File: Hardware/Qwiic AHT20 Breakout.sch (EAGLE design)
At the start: 25 parts, among them J2 QWIIC_RIGHT_ANGLE, J3 PTH, J4 QWIIC_RIGHT_ANGLE, U2 AHT20QFN-6

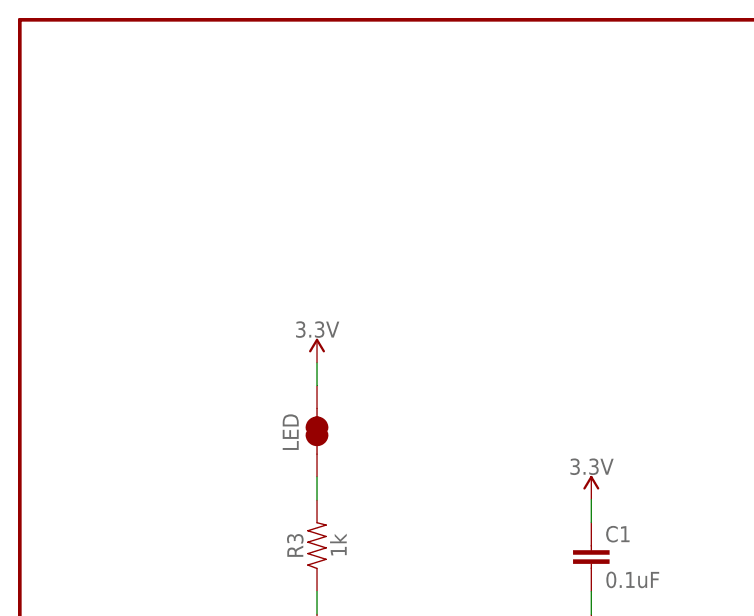
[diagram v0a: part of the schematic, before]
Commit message: Fix FP of IC to correct 2mm pad spacing
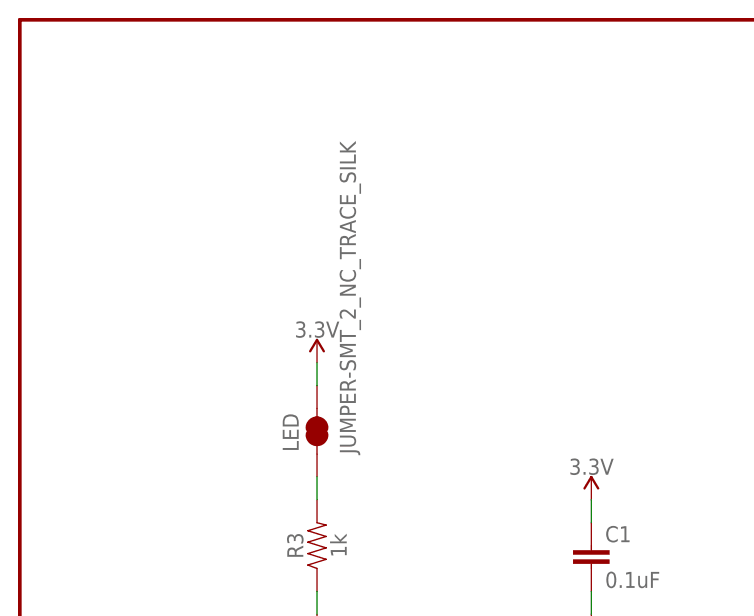
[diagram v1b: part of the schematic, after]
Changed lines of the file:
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@@
 <?xml version="1.0" encoding="utf-8"?>
 <!DOCTYPE eagle SYSTEM "eagle.dtd">
-<eagle version="9.5.2">
+<eagle version="9.6.0">
 <drawing>
 <settings>
@@
 <grid distance="0.1" unitdist="inch" unit="inch" style="lines" multiple="1" display="no" altdistance="0.01" altunitdist="inch" altunit="inch"/>
 <layers>
-<layer number="1" name="Top" color="4" fill="1" visible="yes" active="no"/>
-<layer number="2" name="Route2" color="1" fill="3" visible="yes" active="no"/>
-<layer number="3" name="Route3" color="4" fill="3" visible="yes" active="no"/>
-<layer number="4" name="Route4" color="1" fill="4" visible="yes" active="no"/>
-<layer number="5" name="Route5" color="4" fill="4" visible="yes" active="no"/>
-<layer number="6" name="Route6" color="1" fill="8" visible="yes" active="no"/>
-<layer number="7" name="Route7" color="4" fill="8" visible="yes" active="no"/>
-<layer number="8" name="Route8" color="1" fill="2" visible="yes" active="no"/>
-<layer number="9" name="Route9" color="4" fill="2" visible="yes" active="no"/>
-<layer number="10" name="Route10" color="1" fill="7" visible="yes" active="no"/>
-<layer number="11" name="Route11" color="4" fill="7" visible="yes" active="no"/>
-<layer number="12" name="Route12" color="1" fill="5" visible="yes" active="no"/>
-<layer number="13" name="Route13" color="4" fill="5" visible="yes" active="no"/>
-<layer number="14" name="Route14" color="1" fill="6" visible="yes" active="no"/>
-<layer number="15" name="Route15" color="4" fill="6" visible="yes" active="no"/>
-<layer number="16" name="Bottom" color="1" fill="1" visible="yes" active="no"/>
-<layer number="17" name="Pads" color="2" fill="1" visible="yes" active="no"/>
-<layer number="18" name="Vias" color="2" fill="1" visible="yes" active="no"/>
-<layer number="19" name="Unrouted" color="6" fill="1" visible="yes" active="no"/>
-<layer number="20" name="Dimension" color="24" fill="1" visible="yes" active="no"/>
-<layer number="21" name="tPlace" color="16" fill="1" visible="yes" active="no"/>
-<layer number="22" name="bPlace" color="14" fill="1" visible="yes" active="no"/>
-<layer number="23" name="tOrigins" color="15" fill="1" visible="yes" active="no"/>
-<layer number="24" name="bOrigins" color="15" fill="1" visible="yes" active="no"/>
-<layer number="25" name="tNames" color="7" fill="1" visible="yes" active="no"/>
-<layer number="26" name="bNames" color="7" fill="1" visible="yes" active="no"/>
-<layer number="27" name="tValues" color="7" fill="1" visible="yes" active="no"/>
-<layer number="28" name="bValues" color="7" fill="1" visible="yes" active="no"/>
+<layer number="1" name="Top" color="4" fill="1" visible="no" active="no"/>
+<layer number="2" name="Route2" color="1" fill="3" visible="no" active="no"/>
+<layer number="3" name="Route3" color="4" fill="3" visible="no" active="no"/>
+<layer number="4" name="Route4" color="1" fill="4" visible="no" active="no"/>
+<layer number="5" name="Route5" color="4" fill="4" visible="no" active="no"/>
+<layer number="6" name="Route6" color="1" fill="8" visible="no" active="no"/>
+<layer number="7" name="Route7" color="4" fill="8" visible="no" active="no"/>
+<layer number="8" name="Route8" color="1" fill="2" visible="no" active="no"/>
+<layer number="9" name="Route9" color="4" fill="2" visible="no" active="no"/>
+<layer number="10" name="Route10" color="1" fill="7" visible="no" active="no"/>
+<layer number="11" name="Route11" color="4" fill="7" visible="no" active="no"/>
+<layer number="12" name="Route12" color="1" fill="5" visible="no" active="no"/>
+<layer number="13" name="Route13" color="4" fill="5" visible="no" active="no"/>
+<layer number="14" name="Route14" color="1" fill="6" visible="no" active="no"/>
+<layer number="15" name="Route15" color="4" fill="6" visible="no" active="no"/>
+<layer number="16" name="Bottom" color="1" fill="1" visible="no" active="no"/>
+<layer number="17" name="Pads" color="2" fill="1" visible="no" active="no"/>
+<layer number="18" name="Vias" color="2" fill="1" visible="no" active="no"/>
+<layer number="19" name="Unrouted" color="6" fill="1" visible="no" active="no"/>
+<layer number="20" name="Dimension" color="24" fill="1" visible="no" active="no"/>
+<layer number="21" name="tPlace" color="16" fill="1" visible="no" active="no"/>
+<layer number="22" name="bPlace" color="14" fill="1" visible="no" active="no"/>
+<layer number="23" name="tOrigins" color="15" fill="1" visible="no" active="no"/>
+<layer number="24" name="bOrigins" color="15" fill="1" visible="no" active="no"/>
+<layer number="25" name="tNames" color="7" fill="1" visible="no" active="no"/>
+<layer number="26" name="bNames" color="7" fill="1" visible="no" active="no"/>
+<layer number="27" name="tValues" color="7" fill="1" visible="no" active="no"/>
+<layer number="28" name="bValues" color="7" fill="1" visible="no" active="no"/>
 <layer number="29" name="tStop" color="7" fill="3" visible="no" active="no"/>
 <layer number="30" name="bStop" color="7" fill="6" visible="no" active="no"/>
@@
 <layer number="35" name="tGlue" color="7" fill="4" visible="no" active="no"/>
 <layer number="36" name="bGlue" color="7" fill="5" visible="no" active="no"/>
-<layer number="37" name="tTest" color="7" fill="1" visible="yes" active="no"/>
-<layer number="38" name="bTest" color="7" fill="1" visible="yes" active="no"/>
+<layer number="37" name="tTest" color="7" fill="1" visible="no" active="no"/>
+<layer number="38" name="bTest" color="7" fill="1" visible="no" active="no"/>
 <layer number="39" name="tKeepout" color="4" fill="11" visible="no" active="no"/>
 <layer number="40" name="bKeepout" color="1" fill="11" visible="no" active="no"/>
@@
 <layer number="44" name="Drills" color="7" fill="1" visible="no" active="no"/>
 <layer number="45" name="Holes" color="7" fill="1" visible="no" active="no"/>
-<layer number="46" name="Milling" color="3" fill="1" visible="yes" active="no"/>
-<layer number="47" name="Measures" color="7" fill="1" visible="yes" active="no"/>
-<layer number="48" name="Document" color="7" fill="1" visible="yes" active="no"/>
-<layer number="49" name="Reference" color="7" fill="1" visible="yes" active="no"/>
-<layer number="50" name="dxf" color="7" fill="1" visible="yes" active="no"/>
-<layer number="51" name="tDocu" color="6" fill="1" visible="yes" active="no"/>
-<layer number="52" name="bDocu" color="7" fill="1" visible="yes" active="no"/>
-<layer number="53" name="tGND_GNDA" color="7" fill="9" visible="yes" active="no"/>
-<layer number="54" name="bGND_GNDA" color="1" fill="9" visible="yes" active="no"/>
-<layer number="56" name="wert" color="7" fill="1" visible="yes" active="no"/>
-<layer number="57" name="tCAD" color="7" fill="1" visible="yes" active="no"/>
-<layer number="59" name="tCarbon" color="7" fill="1" visible="yes" active="no"/>
-<layer number="60" name="bCarbon" color="7" fill="1" visible="yes" active="no"/>
+<layer number="46" name="Milling" color="3" fill="1" visible="no" active="no"/>
+<layer number="47" name="Measures" color="7" fill="1" visible="no" active="no"/>
+<layer number="48" name="Document" color="7" fill="1" visible="no" active="no"/>
+<layer number="49" name="Reference" color="7" fill="1" visible="no" active="no"/>
+<layer number="50" name="dxf" color="7" fill="1" visible="no" active="no"/>
+<layer number="51" name="tDocu" color="6" fill="1" visible="no" active="no"/>
+<layer number="52" name="bDocu" color="7" fill="1" visible="no" active="no"/>
+<layer number="53" name="tGND_GNDA" color="7" fill="9" visible="no" active="no"/>
+<layer number="54" name="bGND_GNDA" color="1" fill="9" visible="no" active="no"/>
+<layer number="56" name="wert" color="7" fill="1" visible="no" active="no"/>
+<layer number="57" name="tCAD" color="7" fill="1" visible="no" active="no"/>
+<layer number="59" name="tCarbon" color="7" fill="1" visible="no" active="no"/>
+<layer number="60" name="bCarbon" color="7" fill="1" visible="no" active="no"/>
 <layer number="88" name="SimResults" color="9" fill="1" visible="no" active="yes"/>
 <layer number="89" name="SimProbes" color="9" fill="1" visible="no" active="yes"/>
@@
 <part name="GND5" library="SparkFun-PowerSymbols" deviceset="GND" device=""/>
 <part name="GND6" library="SparkFun-PowerSymbols" deviceset="GND" device=""/>
-<part name="LED" library="SparkFun-Jumpers" deviceset="JUMPER-SMT_2_NC_TRACE" device="_SILK" package3d_urn="urn:adsk.eagle:package:39281/1" value=""/>
+<part name="LED" library="SparkFun-Jumpers" deviceset="JUMPER-SMT_2_NC_TRACE" device="_SILK" package3d_urn="urn:adsk.eagle:package:39281/1" value="JUMPER-SMT_2_NC_TRACE_SILK"/>
 <part name="R4" library="SparkFun-Resistors" deviceset="10KOHM" device="-0603-1/10W-1%" value="10k"/>
 <part name="ADR" library="SparkFun-Jumpers" deviceset="JUMPER-SMT_2_NO" device="_SILK" package3d_urn="urn:adsk.eagle:package:39279/1" value=""/>

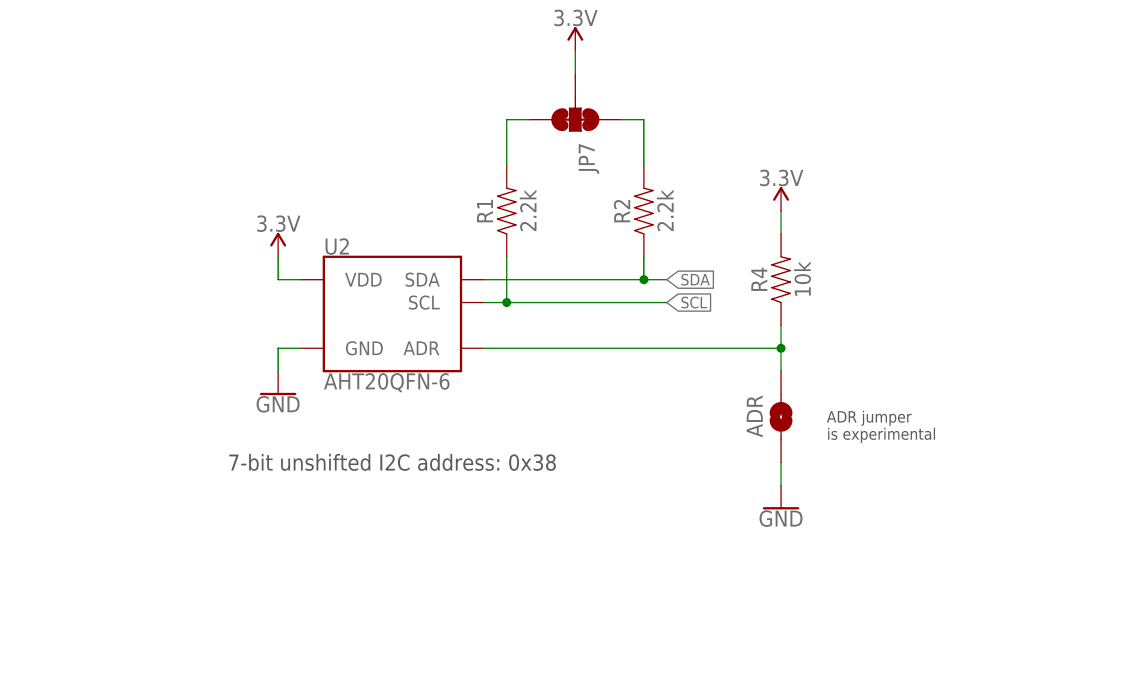
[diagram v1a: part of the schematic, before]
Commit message: Fix FP spacing. Remove experimental ADR feature. Update version number.
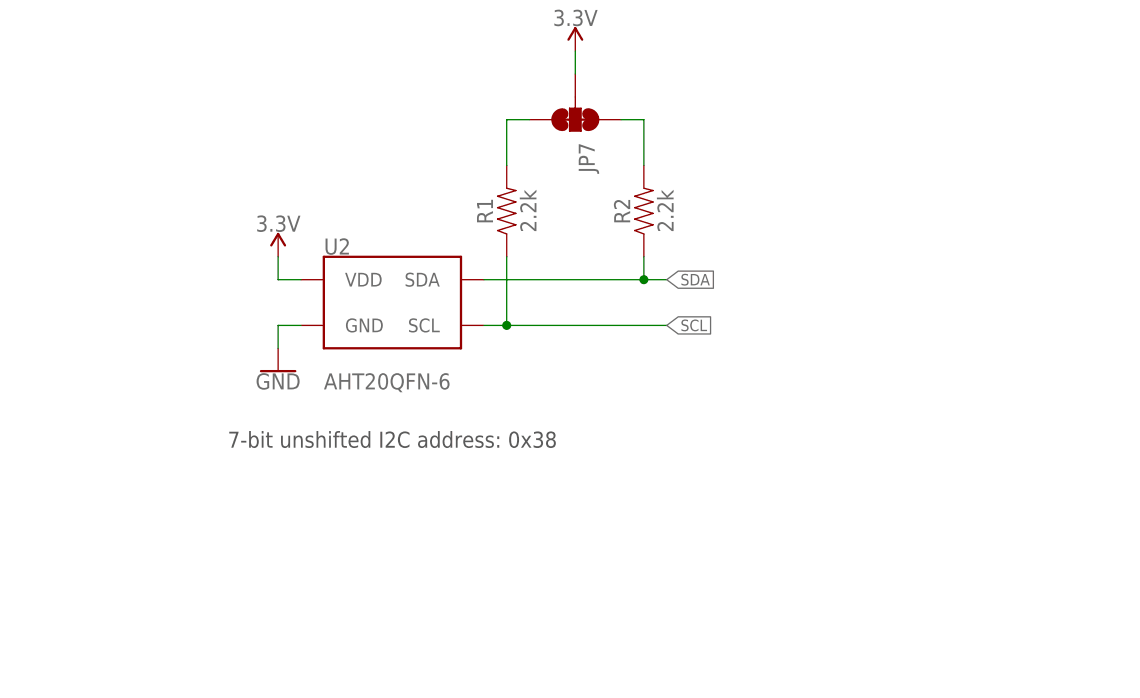
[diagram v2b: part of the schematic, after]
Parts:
- removed ADR: JUMPER-SMT_2_NO_SILK, SparkFun-Jumpers:JUMPER-SMT_2_NO_SILK
- removed R4: 10k, SparkFun-Resistors:10KOHM-0603-1/10W-1%
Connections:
- removed net N$5: ADR.2, R4.1, U2.ADR
- net 3.3V: no longer R4.2
- net GND: no longer ADR.1
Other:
- note removed: "ADR jumper is experimental"
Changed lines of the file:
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@@
 <part name="GND6" library="SparkFun-PowerSymbols" deviceset="GND" device=""/>
 <part name="LED" library="SparkFun-Jumpers" deviceset="JUMPER-SMT_2_NC_TRACE" device="_SILK" package3d_urn="urn:adsk.eagle:package:39281/1" value="JUMPER-SMT_2_NC_TRACE_SILK"/>
-<part name="R4" library="SparkFun-Resistors" deviceset="10KOHM" device="-0603-1/10W-1%" value="10k"/>
-<part name="ADR" library="SparkFun-Jumpers" deviceset="JUMPER-SMT_2_NO" device="_SILK" package3d_urn="urn:adsk.eagle:package:39279/1" value=""/>
 <part name="U2" library="AHT20" deviceset="AHT20" device="QFN-6"/>
-<part name="SUPPLY5" library="SparkFun-PowerSymbols" deviceset="3.3V" device=""/>
-<part name="GND7" library="SparkFun-PowerSymbols" deviceset="GND" device=""/>
 </parts>
 <sheets>
@@
 <plain>
 <text x="237.744" y="7.366" size="2.54" layer="94">x01</text>
-<text x="116.84" y="106.68" size="1.778" layer="97" align="center">7-bit unshifted I2C address: 0x38</text>
+<text x="116.84" y="109.22" size="1.778" layer="97" align="center">7-bit unshifted I2C address: 0x38</text>
 <text x="38.608" y="114.046" size="1.778" layer="97">Power</text>
 <wire x1="0" y1="68.58" x2="248.92" y2="68.58" width="0.2032" layer="97" style="longdash"/>
 <text x="63.5" y="60.96" size="2.54" layer="97" align="center">Connectors</text>
-<text x="165.1" y="109.22" size="1.27" layer="97">ADR jumper
-is experimental</text>
 </plain>
 <instances>
@@
 <attribute name="VALUE" x="63.5" y="116.586" size="1.778" layer="96" align="top-center"/>
 </instance>
-<instance part="GND3" gate="1" x="104.14" y="114.3" smashed="yes">
-<attribute name="VALUE" x="104.14" y="114.046" size="1.778" layer="96" align="top-center"/>
+<instance part="GND3" gate="1" x="104.14" y="116.84" smashed="yes">
+<attribute name="VALUE" x="104.14" y="116.586" size="1.778" layer="96" align="top-center"/>
 </instance>
 <instance part="GND4" gate="1" x="76.2" y="38.1" smashed="yes">
@@
 <attribute name="VALUE" x="35.56" y="137.16" size="1.778" layer="96" font="vector" rot="R90" align="top-left"/>
 </instance>
-<instance part="R4" gate="G$1" x="160.02" y="127" smashed="yes" rot="R90">
-<attribute name="NAME" x="158.496" y="127" size="1.778" layer="95" font="vector" rot="R90" align="bottom-center"/>
-<attribute name="VALUE" x="161.544" y="127" size="1.778" layer="96" font="vector" rot="R90" align="top-center"/>
-</instance>
-<instance part="ADR" gate="G$1" x="160.02" y="111.76" smashed="yes" rot="R90">
-<attribute name="NAME" x="157.988" y="109.474" size="1.778" layer="95" font="vector" rot="R90"/>
-<attribute name="VALUE" x="162.56" y="109.22" size="1.778" layer="96" font="vector" rot="R90" align="top-left"/>
-</instance>
 <instance part="U2" gate="G$1" x="116.84" y="124.46" smashed="yes">
 <attribute name="NAME" x="109.22" y="129.794" size="1.778" layer="95" font="vector"/>
 <attribute name="VALUE" x="109.22" y="116.586" size="1.778" layer="96" font="vector" align="top-left"/>
-</instance>
-<instance part="SUPPLY5" gate="G$1" x="160.02" y="134.62" smashed="yes">
-<attribute name="VALUE" x="160.02" y="137.414" size="1.778" layer="96" align="bottom-center"/>
-</instance>
-<instance part="GND7" gate="1" x="160.02" y="101.6" smashed="yes">
-<attribute name="VALUE" x="160.02" y="101.346" size="1.778" layer="96" align="top-center"/>
 </instance>
 </instances>
@@
 <wire x1="33.02" y1="147.32" x2="33.02" y2="144.78" width="0.1524" layer="91"/>
 </segment>
-<segment>
-<pinref part="R4" gate="G$1" pin="2"/>
-<pinref part="SUPPLY5" gate="G$1" pin="3.3V"/>
-<wire x1="160.02" y1="134.62" x2="160.02" y2="132.08" width="0.1524" layer="91"/>
-</segment>
 </net>
 <net name="SCL" class="0">
@@
 <segment>
 <pinref part="R1" gate="G$1" pin="1"/>
-<wire x1="129.54" y1="129.54" x2="129.54" y2="124.46" width="0.1524" layer="91"/>
-<wire x1="129.54" y1="124.46" x2="127" y2="124.46" width="0.1524" layer="91"/>
-<wire x1="129.54" y1="124.46" x2="147.32" y2="124.46" width="0.1524" layer="91"/>
-<junction x="129.54" y="124.46"/>
-<label x="147.32" y="124.46" size="1.27" layer="95" xref="yes"/>
+<wire x1="129.54" y1="129.54" x2="129.54" y2="121.92" width="0.1524" layer="91"/>
+<wire x1="129.54" y1="121.92" x2="127" y2="121.92" width="0.1524" layer="91"/>
+<wire x1="129.54" y1="121.92" x2="147.32" y2="121.92" width="0.1524" layer="91"/>
+<junction x="129.54" y="121.92"/>
+<label x="147.32" y="121.92" size="1.27" layer="95" xref="yes"/>
 <pinref part="U2" gate="G$1" pin="SCL"/>
 </segment>
@@
 </segment>
 <segment>
-<wire x1="106.68" y1="119.38" x2="104.14" y2="119.38" width="0.1524" layer="91"/>
-<wire x1="104.14" y1="119.38" x2="104.14" y2="116.84" width="0.1524" layer="91"/>
+<wire x1="106.68" y1="121.92" x2="104.14" y2="121.92" width="0.1524" layer="91"/>
+<wire x1="104.14" y1="121.92" x2="104.14" y2="119.38" width="0.1524" layer="91"/>
 <pinref part="GND3" gate="1" pin="GND"/>
 <pinref part="U2" gate="G$1" pin="GND"/>
@@
 <pinref part="GND6" gate="1" pin="GND"/>
 </segment>
-<segment>
-<pinref part="ADR" gate="G$1" pin="1"/>
-<pinref part="GND7" gate="1" pin="GND"/>
-<wire x1="160.02" y1="104.14" x2="160.02" y2="106.68" width="0.1524" layer="91"/>
-</segment>
 </net>
 <net name="N$4" class="0">
@@
 <pinref part="LED" gate="G$1" pin="1"/>
 <wire x1="33.02" y1="134.62" x2="33.02" y2="132.08" width="0.1524" layer="91"/>
-</segment>
-</net>
-<net name="N$5" class="0">
-<segment>
-<pinref part="U2" gate="G$1" pin="ADR"/>
-<pinref part="ADR" gate="G$1" pin="2"/>
-<wire x1="127" y1="119.38" x2="160.02" y2="119.38" width="0.1524" layer="91"/>
-<wire x1="160.02" y1="119.38" x2="160.02" y2="116.84" width="0.1524" layer="91"/>
-<pinref part="R4" gate="G$1" pin="1"/>
-<wire x1="160.02" y1="121.92" x2="160.02" y2="119.38" width="0.1524" layer="91"/>
-<junction x="160.02" y="119.38"/>
 </segment>
 </net>
@@
 </drawing>
 <compatibility>
-<note version="6.3" minversion="6.2.2" severity="warning">
-Since Version 6.2.2 text objects can contain more than one line,
-which will not be processed correctly with this version.
-</note>
 <note version="8.3" severity="warning">
 Since Version 8.3, EAGLE supports URNs for individual library
